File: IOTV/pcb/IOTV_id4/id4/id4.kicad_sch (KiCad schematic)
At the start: 6 parts, among them SW1 SW_Push, SW2 SW_Push, SW3 SW_Push, U1 ESP32_DevKit_V1_DOIT, U2 DFR0299

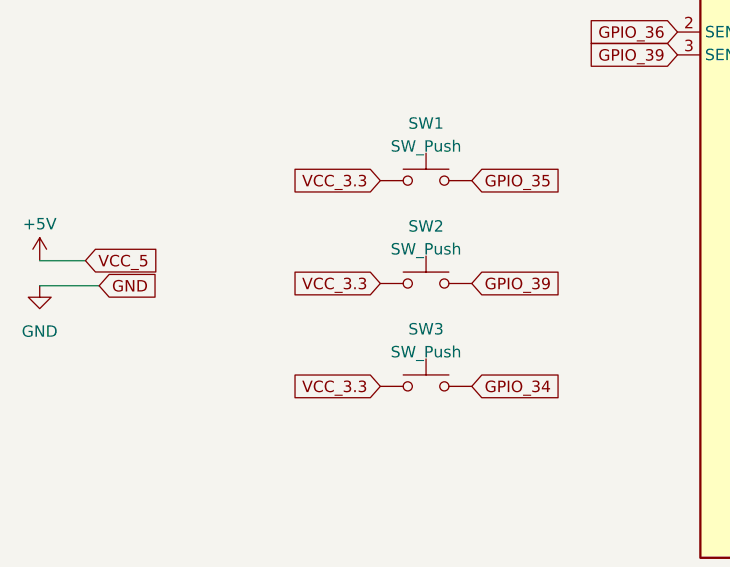
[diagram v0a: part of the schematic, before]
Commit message: PCB id4 кнопки на землю
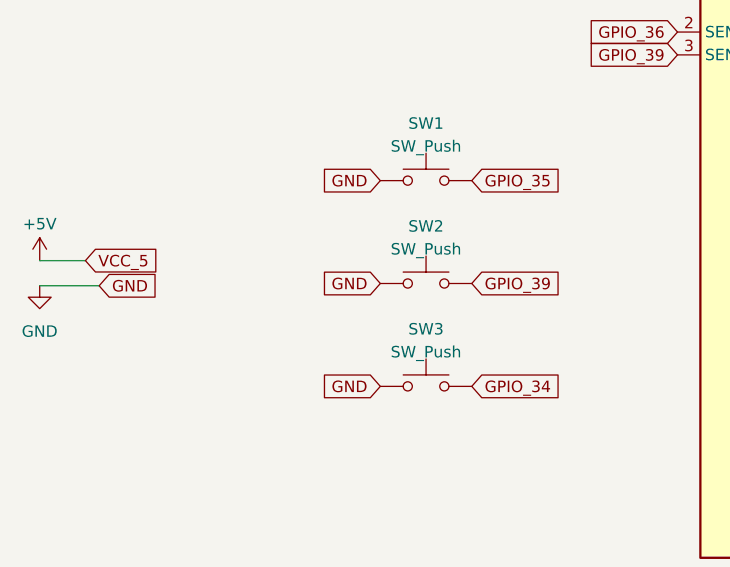
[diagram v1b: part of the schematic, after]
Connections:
- net GND: now also SW1.1, SW2.1, SW3.1
- net VCC_3.3: no longer SW1.1, SW2.1, SW3.1
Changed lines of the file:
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@@
+    )
+  )
+  (global_label "GND" (shape input) (at 66.802 96.012 180) (fields_autoplaced)
+    (effects (font (size 1.27 1.27)) (justify right))
+    (property "Intersheetrefs" "${INTERSHEET_REFS}" (at 60.0257 96.012 0)
+      (effects (font (size 1.27 1.27)) (justify right) hide)
     )
   )
@@
     (property "Intersheetrefs" "${INTERSHEET_REFS}" (at 141.0697 99.822 0)
       (effects (font (size 1.27 1.27)) (justify left) hide)
+    )
+  )
+  (global_label "GND" (shape input) (at 66.802 107.442 180) (fields_autoplaced)
+    (effects (font (size 1.27 1.27)) (justify right))
+    (property "Intersheetrefs" "${INTERSHEET_REFS}" (at 60.0257 107.442 0)
+      (effects (font (size 1.27 1.27)) (justify right) hide)
     )
   )
@@
     (property "Intersheetrefs" "${INTERSHEET_REFS}" (at 141.0697 127.762 0)
       (effects (font (size 1.27 1.27)) (justify left) hide)
-    )
-  )
-  (global_label "VCC_3.3" (shape input) (at 66.802 96.012 180) (fields_autoplaced)
-    (effects (font (size 1.27 1.27)) (justify right))
-    (property "Intersheetrefs" "${INTERSHEET_REFS}" (at 56.2762 96.012 0)
-      (effects (font (size 1.27 1.27)) (justify right) hide)
-    )
-  )
-  (global_label "VCC_3.3" (shape input) (at 66.802 118.872 180) (fields_autoplaced)
-    (effects (font (size 1.27 1.27)) (justify right))
-    (property "Intersheetrefs" "${INTERSHEET_REFS}" (at 56.2762 118.872 0)
-      (effects (font (size 1.27 1.27)) (justify right) hide)
     )
   )
@@
     )
   )
+  (global_label "GND" (shape input) (at 66.802 118.872 180) (fields_autoplaced)
+    (effects (font (size 1.27 1.27)) (justify right))
+    (property "Intersheetrefs" "${INTERSHEET_REFS}" (at 60.0257 118.872 0)
+      (effects (font (size 1.27 1.27)) (justify right) hide)
+    )
+  )
   (global_label "VCC_3.3" (shape input) (at 115.062 69.342 90) (fields_autoplaced)
     (effects (font (size 1.27 1.27)) (justify left))
@@
     )
   )
-  (global_label "VCC_3.3" (shape input) (at 66.802 107.442 180) (fields_autoplaced)
-    (effects (font (size 1.27 1.27)) (justify right))
-    (property "Intersheetrefs" "${INTERSHEET_REFS}" (at 56.2762 107.442 0)
-      (effects (font (size 1.27 1.27)) (justify right) hide)
-    )
-  )
